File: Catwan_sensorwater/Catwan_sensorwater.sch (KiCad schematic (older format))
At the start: 40 parts, among them J1 SENSOR 1, J10 VSP, J2 SENSOR 2, J3 SENSOR 3, J4 BATT, J5 USB_B, J6 Conn_01x04, J7 Conn_01x03, J8 Conn_01x03_Female, J9 SENSOR 4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

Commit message: Add diode and capacitor, food print assignment and list of networks
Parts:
- added C11: 1uF, Capacitor_SMD:C_0805_2012Metric_Pad1.15x1.40mm_HandSolder, symbol Device:C
- added D2: D_Schottky, Diode_SMD:D_0805_2012Metric_Pad1.15x1.40mm_HandSolder, symbol Device:D_Schottky
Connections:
- wire segments 181 -> 184
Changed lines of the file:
@@
 L power:VCC #PWR0112
 U 1 1 5BE4FB31
-P 6675 1324
-F 0 "#PWR0112" H 6675 1174 50  0001 C CNN
-F 1 "VCC" H 6692 1497 50  0000 C CNN
-F 2 "" H 6675 1324 50  0001 C CNN
-F 3 "" H 6675 1324 50  0001 C CNN
-	1    6675 1324
+P 6890 974
+F 0 "#PWR0112" H 6890 824 50  0001 C CNN
+F 1 "VCC" H 6907 1147 50  0000 C CNN
+F 2 "" H 6890 974 50  0001 C CNN
+F 3 "" H 6890 974 50  0001 C CNN
+	1    6890 974
 	1    0    0    -1
 $EndComp
@@
 Wire Wire Line
 	7545 3399 8175 3399
-$Comp
-L power:GND #PWR011
-U 1 1 5BAD7783
-P 3502 1158
-F 0 "#PWR011" H 3502 908 50  0001 C CNN
-F 1 "GND" H 3507 985 50  0000 C CNN
-F 2 "" H 3502 1158 50  0001 C CNN
-F 3 "" H 3502 1158 50  0001 C CNN
-	1    3502 1158
-	1    0    0    -1
-$EndComp
 Wire Notes Line
 	4342 4326 4353 4326
@@
 $EndComp
 Wire Wire Line
-	3116 1073 3502 1073
-Wire Wire Line
-	3502 1073 3502 1158
-Wire Wire Line
 	3116 1173 3293 1173
 Wire Wire Line
@@
 	0    -1   -1   0
 $EndComp
-Wire Wire Line
-	6675 1324 6675 1424
 $Comp
 L Device:C C4
@@
 Wire Wire Line
 	6070 6279 6070 6250
+$Comp
+L Device:C C11
+U 1 1 5C51E879
+P 3566 1073
+F 0 "C11" V 3314 1073 50  0000 C CNN
+F 1 "1uF" V 3405 1073 50  0000 C CNN
+F 2 "Capacitor_SMD:C_0805_2012Metric_Pad1.15x1.40mm_HandSolder" H 3604 923 50  0001 C CNN
+F 3 "~" H 3566 1073 50  0001 C CNN
+	1    3566 1073
+	0    1    1    0
+$EndComp
+Wire Wire Line
+	3116 1073 3416 1073
+$Comp
+L power:GND #PWR011
+U 1 1 5C559755
+P 3754 1164
+F 0 "#PWR011" H 3754 914 50  0001 C CNN
+F 1 "GND" H 3759 991 50  0000 C CNN
+F 2 "" H 3754 1164 50  0001 C CNN
+F 3 "" H 3754 1164 50  0001 C CNN
+	1    3754 1164
+	1    0    0    -1
+$EndComp
+Wire Wire Line
+	3716 1073 3754 1073
+Wire Wire Line
+	3754 1073 3754 1164
+$Comp
+L Device:D_Schottky D2
+U 1 1 5C56404F
+P 6890 1220
+F 0 "D2" V 6942 1436 50  0000 R CNN
+F 1 "D_Schottky" V 6784 1680 50  0000 R CNN
+F 2 "Diode_SMD:D_0805_2012Metric_Pad1.15x1.40mm_HandSolder" H 6890 1220 50  0001 C CNN
+F 3 "~" H 6890 1220 50  0001 C CNN
+	1    6890 1220
+	0    1    1    0
+$EndComp
+Wire Wire Line
+	6675 1424 6890 1424
+Wire Wire Line
+	6890 1370 6890 1424
+Wire Wire Line
+	6890 974  6890 1070
 $EndSCHEMATC

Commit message: Change food print microcontroller
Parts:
- U2: footprint Package_QFP:LQFP-32_7x7mm_P0.8mm -> Package_QFP:TQFP-32_7x7mm_P0.8mm
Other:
- note added: "CHARGER"
- note added: "MODULE LORA\n"
- note removed: "Charger"
- note removed: "MODULATION LORA\n"
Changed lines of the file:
@@
 F 0 "U2" H 2416 3540 50  0000 C CNN
 F 1 "ATSAMD21E18A-MU" H 2416 3449 50  0000 C CNN
-F 2 "Package_QFP:LQFP-32_7x7mm_P0.8mm" H 2416 2173 50  0001 L BNN
+F 2 "Package_QFP:TQFP-32_7x7mm_P0.8mm" H 2416 2173 50  0001 L BNN
 F 3 "SAMD21E Series 256 KB Flash 32 KB SRAM 48 MHz 32-Bit Microcontroller - QFN-32" H 2416 2173 50  0001 L BNN
 F 4 "ATSAMD21E18A-MU-ND" H 2416 2173 50  0001 L BNN "Campo4"
@@
 POWER SUPPLY
 Text Notes 542  4480 0    50   ~ 0
-MODULATION LORA\n
+MODULE LORA\n
 Text Notes 7058 4468 0    50   ~ 0
 SENSORES\n
@@
 	6401 4546 6401 4682
 Text Notes 3928 4460 0    50   ~ 0
-Charger
+CHARGER
 Wire Notes Line
 	6964 6532 6964 4332

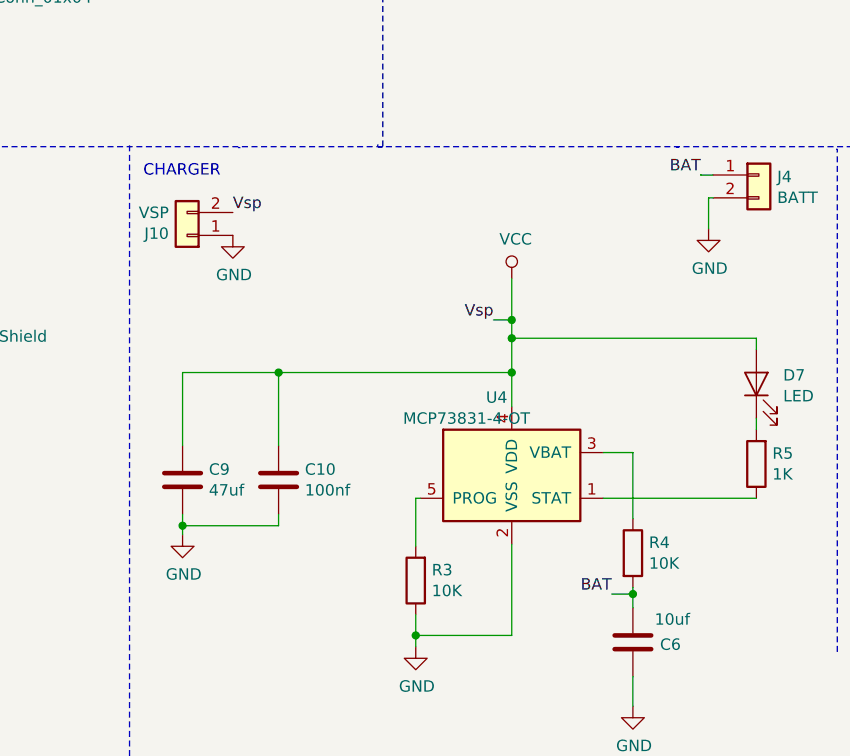
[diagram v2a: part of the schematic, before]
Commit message: Add diodes in vsp, remove capacitor and 10k resistance
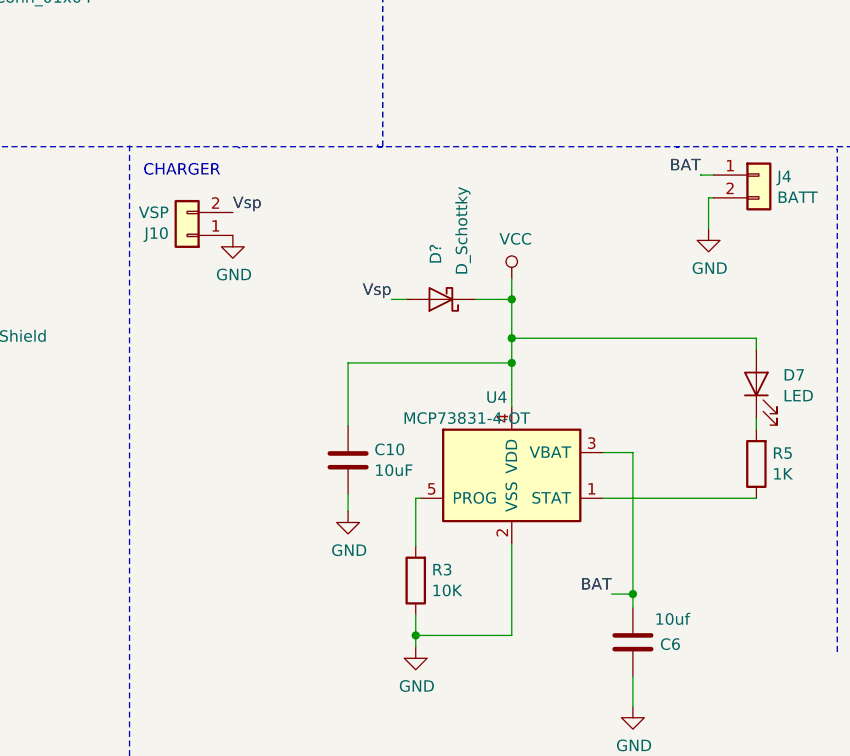
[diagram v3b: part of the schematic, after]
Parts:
- removed C9: 47uf, Capacitor_SMD:C_0805_2012Metric_Pad1.15x1.40mm_HandSolder, symbol Device:C
- removed R4: 10K, Resistor_SMD:R_0805_2012Metric_Pad1.15x1.40mm_HandSolder, symbol Device:R
- added D?: D_Schottky, Diode_SMD:D_0805_2012Metric_Pad1.15x1.40mm_HandSolder, symbol Device:D_Schottky
- C10: value 100nf -> 10uF
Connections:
- wire segments 184 -> 179
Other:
- moved on the sheet: C10
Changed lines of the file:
@@
-$EndComp
-$Comp
-L Device:R R4
-U 1 1 5BC24D96
-P 6070 6100
-F 0 "R4" H 6140 6146 50  0000 L CNN
-F 1 "10K" H 6140 6055 50  0000 L CNN
-F 2 "Resistor_SMD:R_0805_2012Metric_Pad1.15x1.40mm_HandSolder" V 6000 6100 50  0001 C CNN
-F 3 "~" H 6070 6100 50  0001 C CNN
-	1    6070 6100
-	1    0    0    -1
 $EndComp
 $Comp
@@
 	11224 2695 11224 2706
 $Comp
-L Device:C C9
-U 1 1 5BF450D9
-P 4100 5780
-F 0 "C9" H 4215 5826 50  0000 L CNN
-F 1 "47uf" H 4215 5735 50  0000 L CNN
-F 2 "Capacitor_SMD:C_0805_2012Metric_Pad1.15x1.40mm_HandSolder" H 4138 5630 50  0001 C CNN
-F 3 "~" H 4100 5780 50  0001 C CNN
-	1    4100 5780
-	1    0    0    -1
-$EndComp
-$Comp
-L Device:C C10
-U 1 1 5BF45235
-P 4520 5780
-F 0 "C10" H 4635 5826 50  0000 L CNN
-F 1 "100nf" H 4635 5735 50  0000 L CNN
-F 2 "Capacitor_SMD:C_0805_2012Metric_Pad1.15x1.40mm_HandSolder" H 4558 5630 50  0001 C CNN
-F 3 "~" H 4520 5780 50  0001 C CNN
-	1    4520 5780
-	1    0    0    -1
-$EndComp
-$Comp
-L power:GND #PWR0114
-U 1 1 5BFB79E0
-P 4100 6020
-F 0 "#PWR0114" H 4100 5770 50  0001 C CNN
-F 1 "GND" H 4105 5847 50  0000 C CNN
-F 2 "" H 4100 6020 50  0001 C CNN
-F 3 "" H 4100 6020 50  0001 C CNN
-	1    4100 6020
-	1    0    0    -1
-$EndComp
-$Comp
 L Device:C C8
 U 1 1 5BEB65DE
@@
 	1    0    0    -1
 $EndComp
-Text Label 5460 5080 2    50   ~ 0
+Text Label 5014 4990 2    50   ~ 0
 Vsp
 $Comp
@@
 	1    0    0    -1
 $EndComp
-Wire Wire Line
-	5540 4900 5540 5080
-Wire Wire Line
-	5460 5080 5540 5080
-Connection ~ 5540 5080
 $Comp
 L Device:LED D7
@@
 	6610 5510 6610 5560
 Wire Wire Line
-	5540 5080 5540 5160
-Wire Wire Line
 	6610 5860 5940 5860
 Wire Wire Line
@@
 Connection ~ 5540 5160
 Wire Wire Line
-	5540 5160 5540 5310
-Wire Wire Line
 	5940 5660 6070 5660
-Wire Wire Line
-	6070 5660 6070 5950
 $Comp
 L Device:C C6
@@
 	5120 5860 5120 6070
 Wire Wire Line
-	4100 5630 4100 5310
-Wire Wire Line
-	4100 5310 4520 5310
-Connection ~ 5540 5310
-Wire Wire Line
-	5540 5310 5540 5460
-Wire Wire Line
-	4520 5630 4520 5310
-Connection ~ 4520 5310
-Wire Wire Line
-	4520 5310 5540 5310
-Wire Wire Line
-	4100 5930 4100 5980
-Wire Wire Line
-	4520 5930 4520 5980
-Wire Wire Line
-	4520 5980 4100 5980
-Connection ~ 4100 5980
-Wire Wire Line
-	4100 5980 4100 6020
-Wire Wire Line
 	6070 6340 6070 6279
 Wire Wire Line
@@
 	5977 6279 6070 6279
 Connection ~ 6070 6279
-Wire Wire Line
-	6070 6279 6070 6250
 $Comp
 L Device:C C11
@@
 Wire Wire Line
 	6890 974  6890 1070
+Wire Wire Line
+	6070 5660 6070 6279
+Wire Wire Line
+	5540 4900 5540 4990
+$Comp
+L Device:D_Schottky D?
+U 1 1 5C536A87
+P 5230 4990
+F 0 "D?" V 5252 4836 50  0000 R CNN
+F 1 "D_Schottky" V 5138 4884 50  0000 R CNN
+F 2 "Diode_SMD:D_0805_2012Metric_Pad1.15x1.40mm_HandSolder" H 5230 4990 50  0001 C CNN
+F 3 "~" H 5230 4990 50  0001 C CNN
+	1    5230 4990
+	-1   0    0    1
+$EndComp
+Wire Wire Line
+	5380 4990 5540 4990
+Connection ~ 5540 4990
+Wire Wire Line
+	5540 4990 5540 5160
+Wire Wire Line
+	5014 4990 5080 4990
+$Comp
+L power:GND #PWR0114
+U 1 1 5BFB79E0
+P 4824 5916
+F 0 "#PWR0114" H 4824 5666 50  0001 C CNN
+F 1 "GND" H 4829 5743 50  0000 C CNN
+F 2 "" H 4824 5916 50  0001 C CNN
+F 3 "" H 4824 5916 50  0001 C CNN
+	1    4824 5916
+	1    0    0    -1
+$EndComp
+Wire Wire Line
+	5540 5160 5540 5268
+Wire Wire Line
+	5540 5268 4824 5268
+Wire Wire Line
+	4824 5268 4824 5544
+Connection ~ 5540 5268
+Wire Wire Line
+	5540 5268 5540 5460
+$Comp
+L Device:C C10
+U 1 1 5BF45235
+P 4824 5694
+F 0 "C10" H 4939 5740 50  0000 L CNN
+F 1 "10uF" H 4939 5649 50  0000 L CNN
+F 2 "Capacitor_SMD:C_0805_2012Metric_Pad1.15x1.40mm_HandSolder" H 4862 5544 50  0001 C CNN
+F 3 "~" H 4824 5694 50  0001 C CNN
+	1    4824 5694
+	1    0    0    -1
+$EndComp
+Wire Wire Line
+	4824 5844 4824 5916
 $EndSCHEMATC

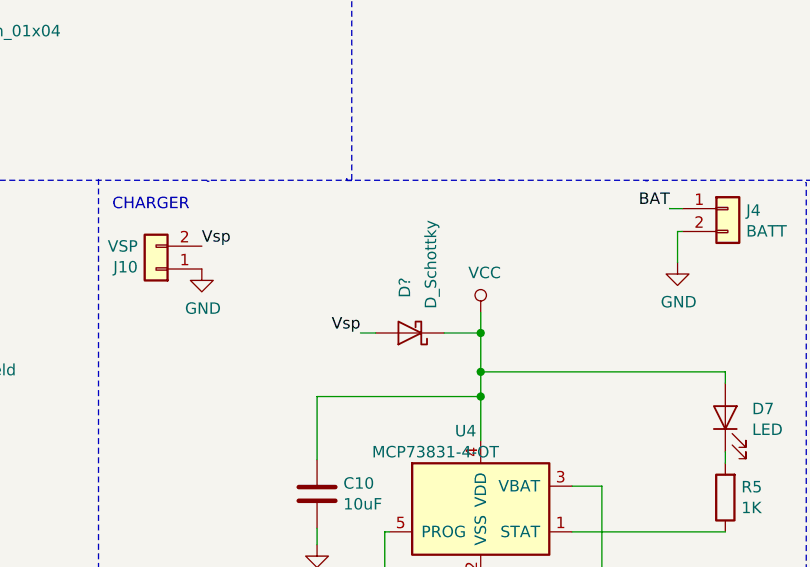
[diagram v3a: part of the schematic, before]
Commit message: Add foodprint D3
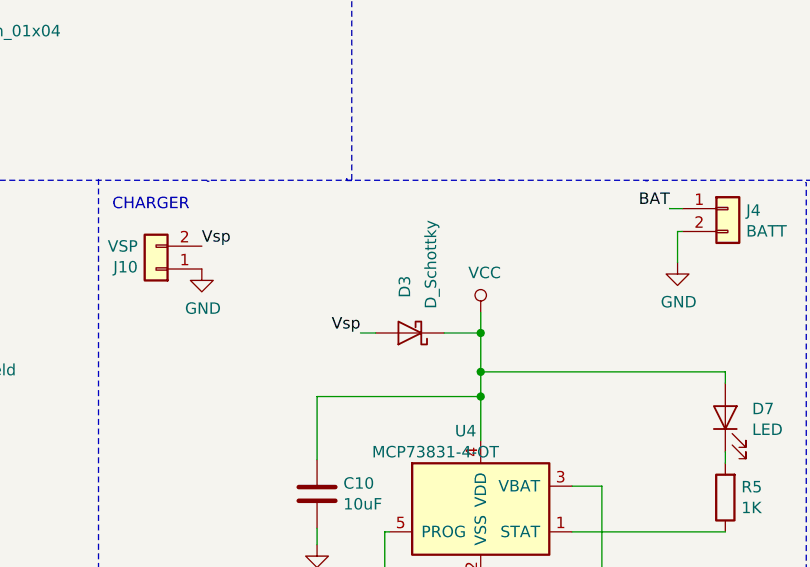
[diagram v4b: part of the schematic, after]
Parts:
- gave numbers to parts that had none: 1
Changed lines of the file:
@@
 	5540 4900 5540 4990
 $Comp
-L Device:D_Schottky D?
+L Device:D_Schottky D3
 U 1 1 5C536A87
 P 5230 4990
-F 0 "D?" V 5252 4836 50  0000 R CNN
+F 0 "D3" V 5252 4836 50  0000 R CNN
 F 1 "D_Schottky" V 5138 4884 50  0000 R CNN
 F 2 "Diode_SMD:D_0805_2012Metric_Pad1.15x1.40mm_HandSolder" H 5230 4990 50  0001 C CNN

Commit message: changes foodprint diode
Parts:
- D1, D2, D3: footprint Diode_SMD:D_0805_2012Metric_Pad1.15x1.40mm_HandSolder -> Diode_SMD:D_SOD-123
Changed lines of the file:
@@
 F 0 "D1" V 7626 1351 50  0000 R CNN
 F 1 "D_Schottky" V 7535 1351 50  0000 R CNN
-F 2 "Diode_SMD:D_0805_2012Metric_Pad1.15x1.40mm_HandSolder" H 7580 1430 50  0001 C CNN
+F 2 "Diode_SMD:D_SOD-123" H 7580 1430 50  0001 C CNN
 F 3 "~" H 7580 1430 50  0001 C CNN
 	1    7580 1430
@@
 F 0 "D2" V 6942 1436 50  0000 R CNN
 F 1 "D_Schottky" V 6784 1680 50  0000 R CNN
-F 2 "Diode_SMD:D_0805_2012Metric_Pad1.15x1.40mm_HandSolder" H 6890 1220 50  0001 C CNN
+F 2 "Diode_SMD:D_SOD-123" H 6890 1220 50  0001 C CNN
 F 3 "~" H 6890 1220 50  0001 C CNN
 	1    6890 1220
@@
 F 0 "D3" V 5252 4836 50  0000 R CNN
 F 1 "D_Schottky" V 5138 4884 50  0000 R CNN
-F 2 "Diode_SMD:D_0805_2012Metric_Pad1.15x1.40mm_HandSolder" H 5230 4990 50  0001 C CNN
+F 2 "Diode_SMD:D_SOD-123" H 5230 4990 50  0001 C CNN
 F 3 "~" H 5230 4990 50  0001 C CNN
 	1    5230 4990

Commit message: remove serial port
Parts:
- removed J7: Conn_01x03, Connector_PinHeader_2.54mm:PinHeader_1x03_P2.54mm_Vertical, symbol Connector_Generic:Conn_01x03
- U2: symbol electroniccats:ATSAMD21E18A-MU -> Catwan_sensorwater-rescue:ATSAMD21E18A-MU-electroniccats
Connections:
- net labels added: +5V
- net labels removed: Rx, Tx, Vsp
- wire segments 179 -> 180
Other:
- note added: "Batterie and charger"
- note added: "Solar Cell"
- note removed: "CHARGER"
- moved on the sheet: C2, C4, C5, D1, D10, D2, J10, J4, J5, J8, R6, U1

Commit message: new  netlist and accommodation
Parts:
- U2: symbol Catwan_sensorwater-rescue:ATSAMD21E18A-MU-electroniccats -> Catwan_sensorwater-rescue:ATSAMD21E18A-MU-electroniccats-Catwan_sensorwater-rescue
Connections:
- wire segments 180 -> 178
- no-connect marks 7 -> 9
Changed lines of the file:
@@
 Wire Wire Line
 	1716 2373 1570 2373
-Wire Wire Line
-	1716 2673 1638 2673
-Wire Wire Line
-	1716 2773 1630 2773
 Text Label 3089 3744 3    50   ~ 0
 SWCLK
@@
 $EndComp
 $Comp
-L Catwan_sensorwater-rescue:ATSAMD21E18A-MU-electroniccats U2
+L Catwan_sensorwater-rescue:ATSAMD21E18A-MU-electroniccats-Catwan_sensorwater-rescue U2
 U 1 1 5BAD6569
 P 2416 2173
@@
 	1    0    0    -1
 $EndComp
+NoConn ~ 1716 2773
+NoConn ~ 1716 2673
 $EndSCHEMATC

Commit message: add RTC and ADC Battery
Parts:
- added C12, C9: 0.1uF, Capacitors_SMD:C_0805_HandSoldering, symbol Device:C_Small
- added R4, R7: 100K, Resistors_SMD:R_0805_HandSoldering, symbol Device:R_Small
- added Y1: 32.768Khz, Crystals:Crystal_AT310_d3.0mm_l10.0mm_Vertical, symbol Device:Crystal_Small
- D7: value LED -> CHG
- R5: footprint Resistor_SMD:R_0805_2012Metric_Pad1.15x1.40mm_HandSolder -> Resistors_SMD:R_0805_HandSoldering
- U2: symbol Catwan_sensorwater-rescue:ATSAMD21E18A-MU-electroniccats-Catwan_sensorwater-rescue -> Catwan_sensorwater-rescue:ATSAMD21E18A-MU-electroniccats-Catwan_sensorwater-rescue-Catwan_sensorwater-rescue
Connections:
- net labels added: ADC_BAT, Y1, Y2
- wire segments 178 -> 195
- no-connect marks 9 -> 6
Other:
- moved on the sheet: C7, D2, J5
